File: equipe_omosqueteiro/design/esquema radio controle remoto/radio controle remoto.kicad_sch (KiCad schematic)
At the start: 18 parts, among them J1 Screw_Terminal_01x02, J2 Conn_01x04_Socket, U3 StepDown_LM2596HV, U4 LM1117T-3.3

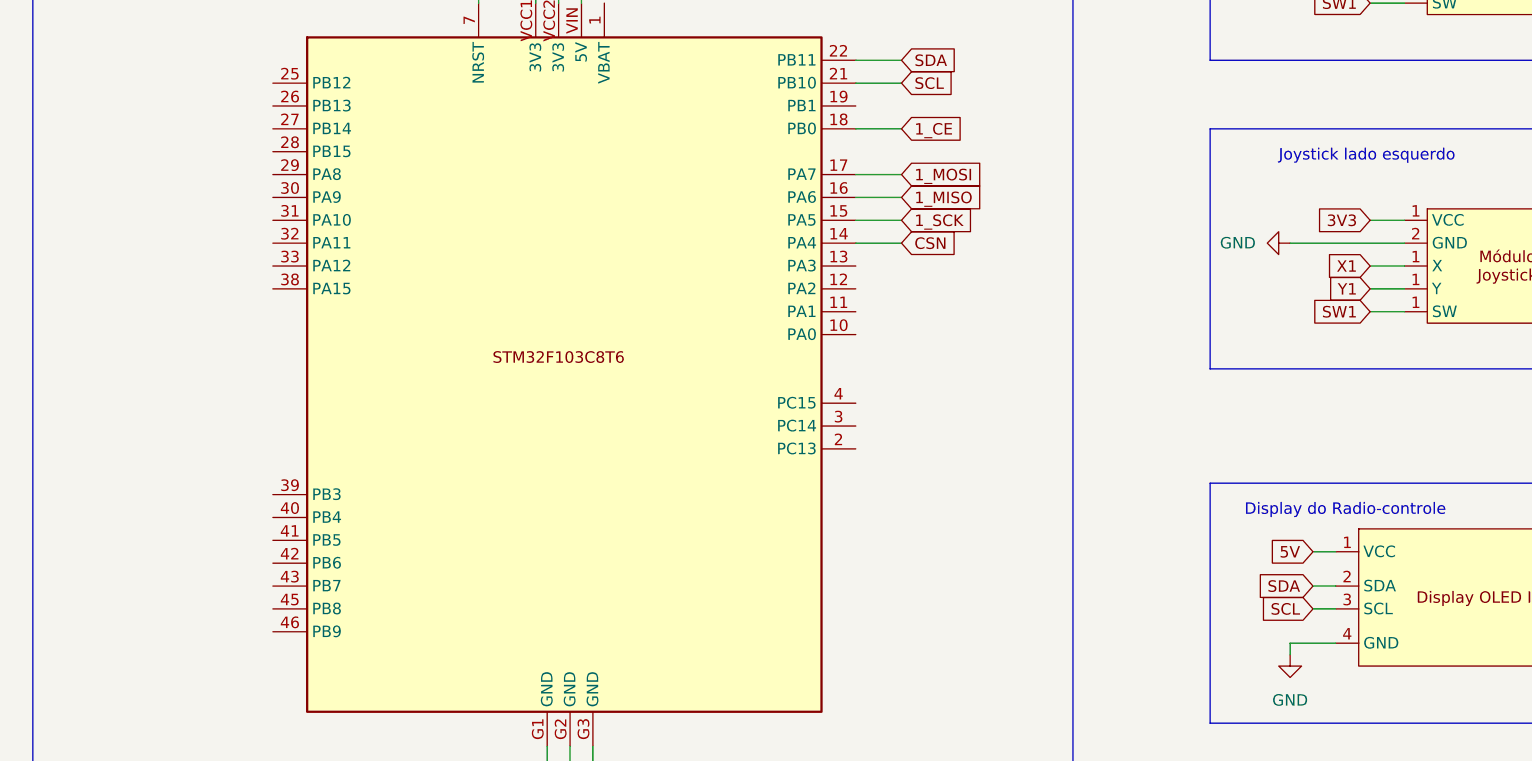
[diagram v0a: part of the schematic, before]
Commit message: adicionado diagramas e texto design
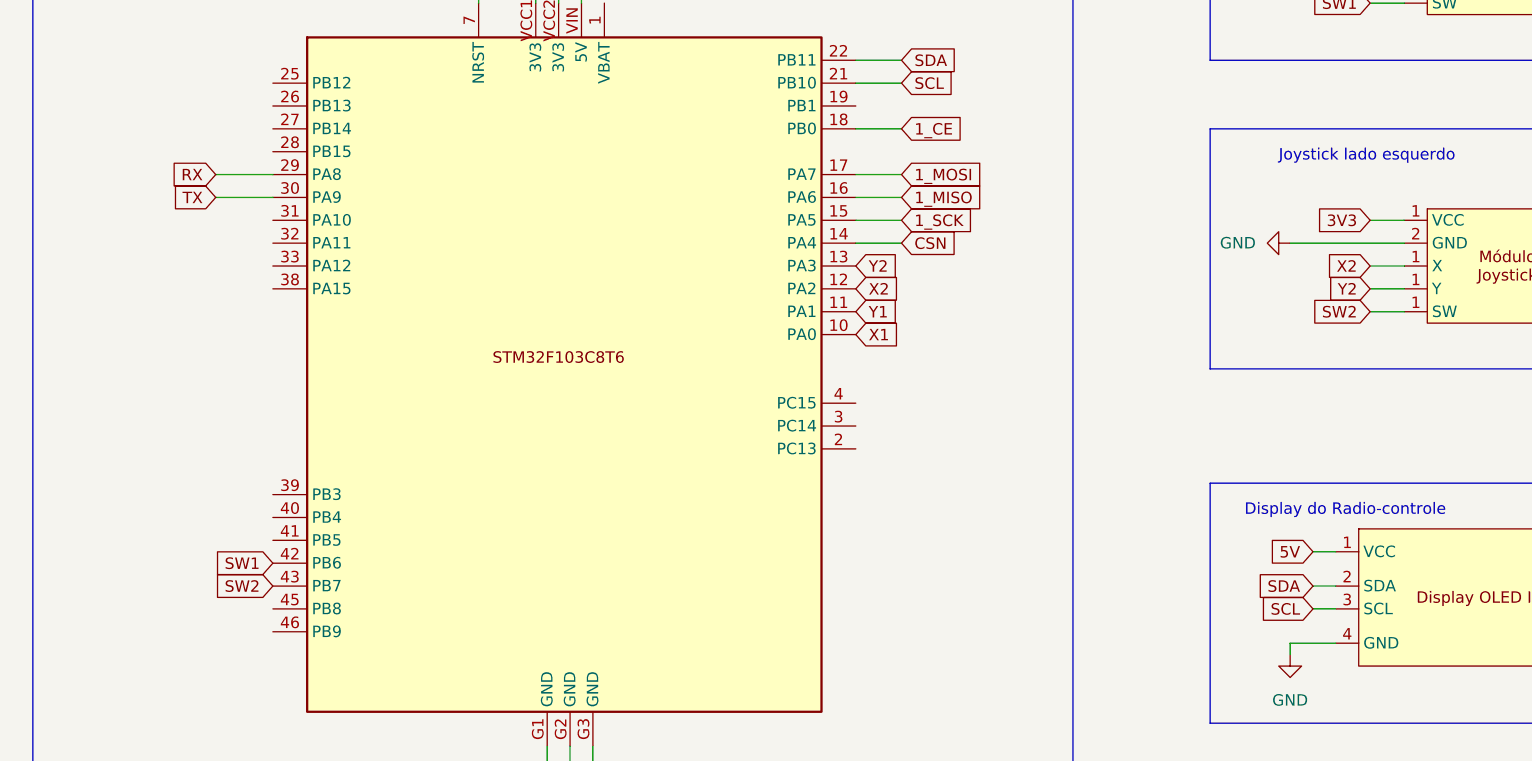
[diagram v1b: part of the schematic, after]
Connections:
- net RX: now also U5.29 (PA8)
- net SW1: now also U5.42 (PB6); no longer U6.1 (Y)
- net TX: now also U5.30 (PA9)
- net X1: now also U5.10 (PA0); no longer U6.1 (Y)
- net Y1: now also U5.11 (PA1); no longer U6.1 (Y)
- net X2: now reaches U5.12 (PA2)
- net X2: now also U6.1 (Y)
- net Y2: now reaches U5.13 (PA3)
- net Y2: now also U6.1 (Y)
- net SW2: now reaches U5.43 (PB7)
- net SW2: now also U6.1 (Y)
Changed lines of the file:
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@@
+    (stroke (width 0) (type default))
+  )
+  (wire (pts (xy 157.48 137.16) (xy 163.83 137.16))
     (stroke (width 0) (type default))
   )
@@
     (stroke (width 0) (type default))
   )
+  (wire (pts (xy 157.48 139.7) (xy 163.83 139.7))
+    (stroke (width 0) (type default))
+  )
   (polyline (pts (xy 45.72 82.55) (xy 46.99 82.55))
     (stroke (width 0) (type default))
@@
     (effects (font (size 1.27 1.27)) (justify left bottom))
   )
-  (global_label "Y1" (shape input) (at 285.75 149.86 180) (fields_autoplaced)
+  (global_label "TX" (shape input) (at 157.48 139.7 180) (fields_autoplaced)
+    (effects (font (size 1.27 1.27)) (justify right))
+    (property "Intersheetrefs" "${INTERSHEET_REFS}" (at 152.3177 139.7 0)
+      (effects (font (size 1.27 1.27)) (justify right) hide)
+    )
+  )
+  (global_label "Y2" (shape input) (at 285.75 149.86 180) (fields_autoplaced)
     (effects (font (size 1.27 1.27)) (justify right))
     (property "Intersheetrefs" "${INTERSHEET_REFS}" (at 280.4667 149.86 0)
@@
     )
   )
+  (global_label "X2" (shape input) (at 228.6 149.86 0) (fields_autoplaced)
+    (effects (font (size 1.27 1.27)) (justify left))
+    (property "Intersheetrefs" "${INTERSHEET_REFS}" (at 234.0042 149.86 0)
+      (effects (font (size 1.27 1.27)) (justify left) hide)
+    )
+  )
+  (global_label "X1" (shape input) (at 228.6 154.94 0) (fields_autoplaced)
+    (effects (font (size 1.27 1.27)) (justify left))
+    (property "Intersheetrefs" "${INTERSHEET_REFS}" (at 234.0042 154.94 0)
+      (effects (font (size 1.27 1.27)) (justify left) hide)
+    )
+  )
+  (global_label "Y1" (shape input) (at 228.6 152.4 0) (fields_autoplaced)
+    (effects (font (size 1.27 1.27)) (justify left))
+    (property "Intersheetrefs" "${INTERSHEET_REFS}" (at 233.8833 152.4 0)
+      (effects (font (size 1.27 1.27)) (justify left) hide)
+    )
+  )
   (global_label "3V3" (shape input) (at 195.58 107.95 90) (fields_autoplaced)
     (effects (font (size 1.27 1.27)) (justify left))
@@
     )
   )
-  (global_label "X1" (shape input) (at 285.75 147.32 180) (fields_autoplaced)
+  (global_label "X2" (shape input) (at 285.75 147.32 180) (fields_autoplaced)
     (effects (font (size 1.27 1.27)) (justify right))
     (property "Intersheetrefs" "${INTERSHEET_REFS}" (at 280.3458 147.32 0)
@@
     )
   )
-  (global_label "SW1" (shape input) (at 285.75 152.4 180) (fields_autoplaced)
+  (global_label "SW2" (shape input) (at 285.75 152.4 180) (fields_autoplaced)
     (effects (font (size 1.27 1.27)) (justify right))
     (property "Intersheetrefs" "${INTERSHEET_REFS}" (at 278.8944 152.4 0)
@@
     )
   )
+  (global_label "SW2" (shape input) (at 163.83 182.88 180) (fields_autoplaced)
+    (effects (font (size 1.27 1.27)) (justify right))
+    (property "Intersheetrefs" "${INTERSHEET_REFS}" (at 156.9744 182.88 0)
+      (effects (font (size 1.27 1.27)) (justify right) hide)
+    )
+  )
   (global_label "RX" (shape input) (at 55.88 193.04 180) (fields_autoplaced)
     (effects (font (size 1.27 1.27)) (justify right))
@@
     )
   )
+  (global_label "SW1" (shape input) (at 163.83 180.34 180) (fields_autoplaced)
+    (effects (font (size 1.27 1.27)) (justify right))
+    (property "Intersheetrefs" "${INTERSHEET_REFS}" (at 156.9744 180.34 0)
+      (effects (font (size 1.27 1.27)) (justify right) hide)
+    )
+  )
   (global_label "5V" (shape input) (at 53.34 184.15 90) (fields_autoplaced)
     (effects (font (size 1.27 1.27)) (justify left))
@@
     )
   )
+  (global_label "Y2" (shape input) (at 228.6 147.32 0) (fields_autoplaced)
+    (effects (font (size 1.27 1.27)) (justify left))
+    (property "Intersheetrefs" "${INTERSHEET_REFS}" (at 233.8833 147.32 0)
+      (effects (font (size 1.27 1.27)) (justify left) hide)
+    )
+  )
   (global_label "SCL" (shape input) (at 233.68 127 0) (fields_autoplaced)
     (effects (font (size 1.27 1.27)) (justify left))
@@
     )
   )
+  (global_label "RX" (shape input) (at 157.48 137.16 180) (fields_autoplaced)
+    (effects (font (size 1.27 1.27)) (justify right))
+    (property "Intersheetrefs" "${INTERSHEET_REFS}" (at 152.0153 137.16 0)
+      (effects (font (size 1.27 1.27)) (justify right) hide)
+    )
+  )
